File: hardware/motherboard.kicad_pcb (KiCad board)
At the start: 2 copper layers, 200 x 150 mm, 305 parts, among them J1 24 V DC input, J10 AX0: EN, STEP, DIR, GND, J11 AX1: EN, STEP, DIR, GND, J12 General outputs 0-7; pin9 fie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, J13 Encoder 0: +5,A,B,Z,GND, J14 Encoder 1: +5,A,B,Z,GND, J15 Encoder 2: +5,A,B,Z,GND, J16 Keyboard KIN0-7 / KOUT0-7, J17 Keyboard power/reference, J18 I2C0, J19 Full-size SD, SPI, J20 ESP-01S socket, J22 LCD LVDS 2x10, 2.00 mm, J23 HDMI Type A, J24 AI0/GND/AI1/GND/AI2/GND, J25 0-10 V outputs 0-3; pin 1 = c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, J26 Dedicated START button input, J27 Expansion inputs 4-7; 1=GND, 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, J28 AX2: EN, STEP, DIR, GND, J29 AX3: EN, STEP, DIR, GND, J30 AX4: EN, STEP, DIR, GND, J31 Motion AUX open-drain output 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, J4 SWD, J5 Dedicated E-stop loop, J6 Dedicated HOLD button input, J7 PLC inputs 1-8; alternating i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, J8 PLC inputs 9-16; alternating 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, J9 Expansion inputs 0-3; 1=GND, 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, Q1 DMP1045U-7, Q5 BSS138, SW2 ESP_PROG, U1 LMR36510ADDAR, U10 74HC595D, U11 74HC595D, U12 74HC595D, U13 74HC595D, U18 LTV-847S, U19 LTV-847S, U2 AMS1117-3.3, U20 LTV-847S, U21 LTV-847S, U24 SN74AHCT541DW, U25 SN74AHCT541DW, U26 ULN2003ADR, U27 ULN2003ADR, U28 SN74AHCT541DW, U30 TPD4E05U06DQA, U31 TPD4E05U06DQA, U32 TPD4E05U06DQA, U34 AMS1117-3.3, U35 EL3H7, U36 EL3H7, U37 L78L12ACUTR, U38 TLV2374IDR, U39 EL3H7, U40 TBA2-0512, U6 74HC165D, U7 74HC165D, U8 74HC165D, U9 74HC165D

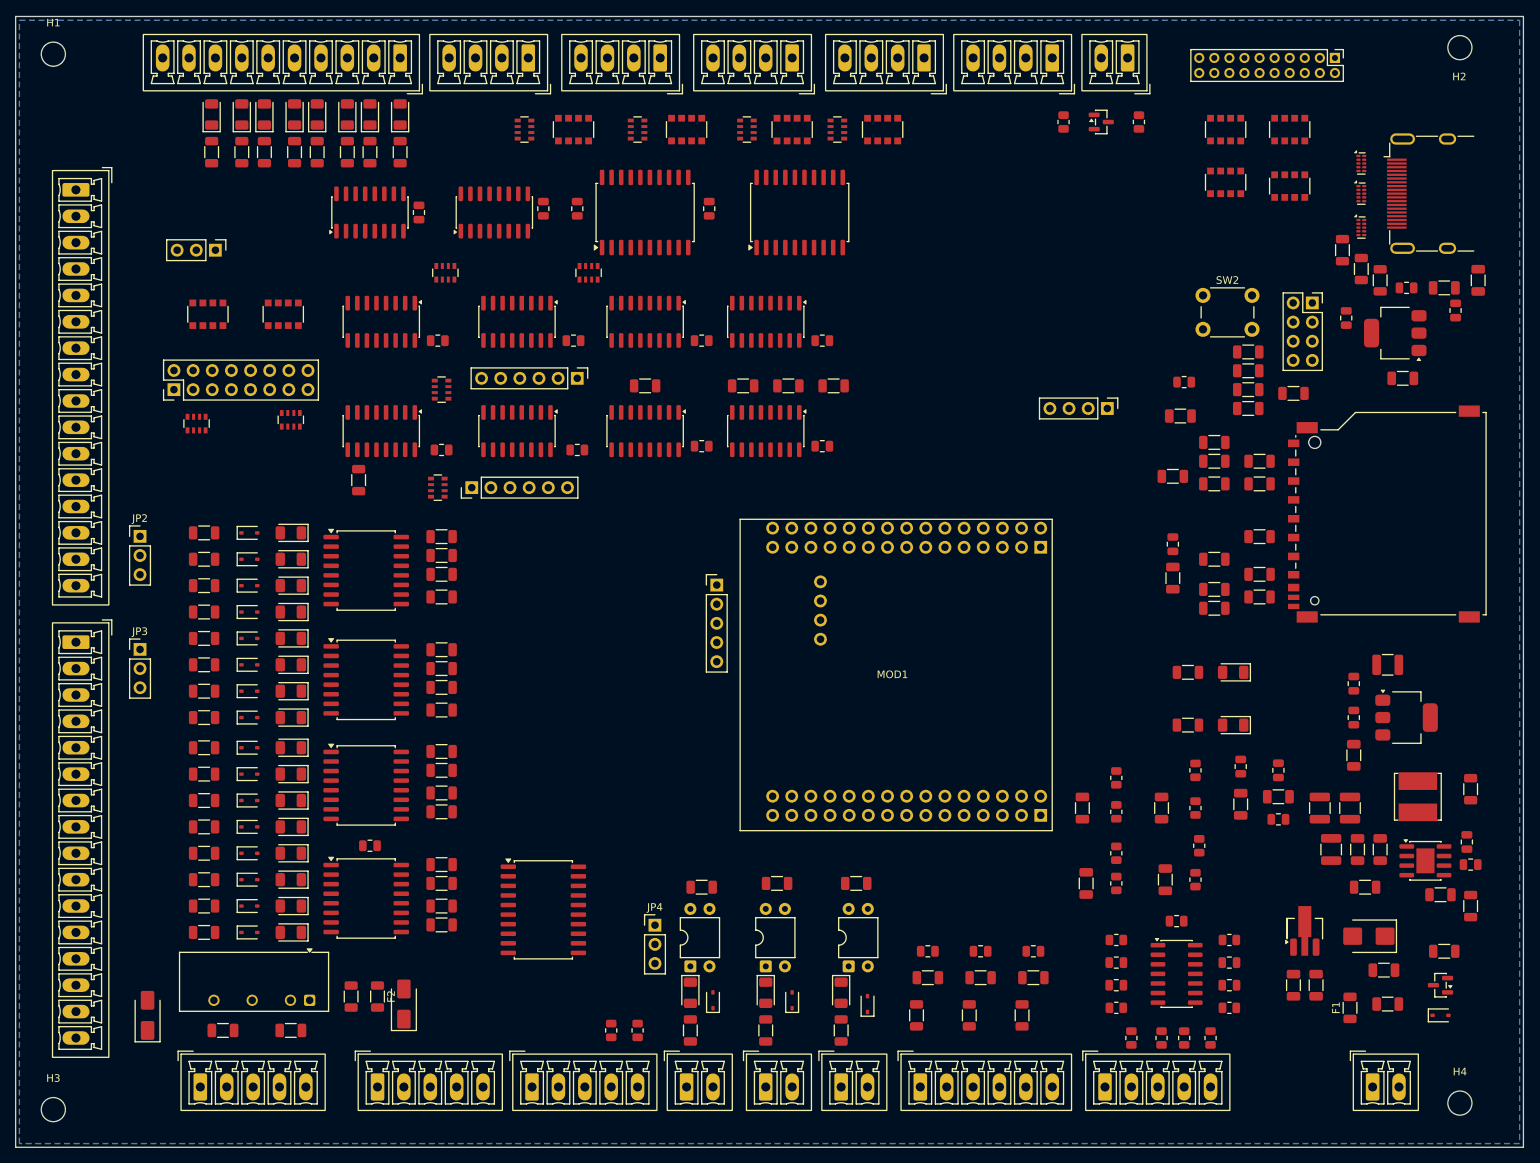
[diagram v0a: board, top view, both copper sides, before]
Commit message: Update RP2350B PCB, pinout and fabrication rules
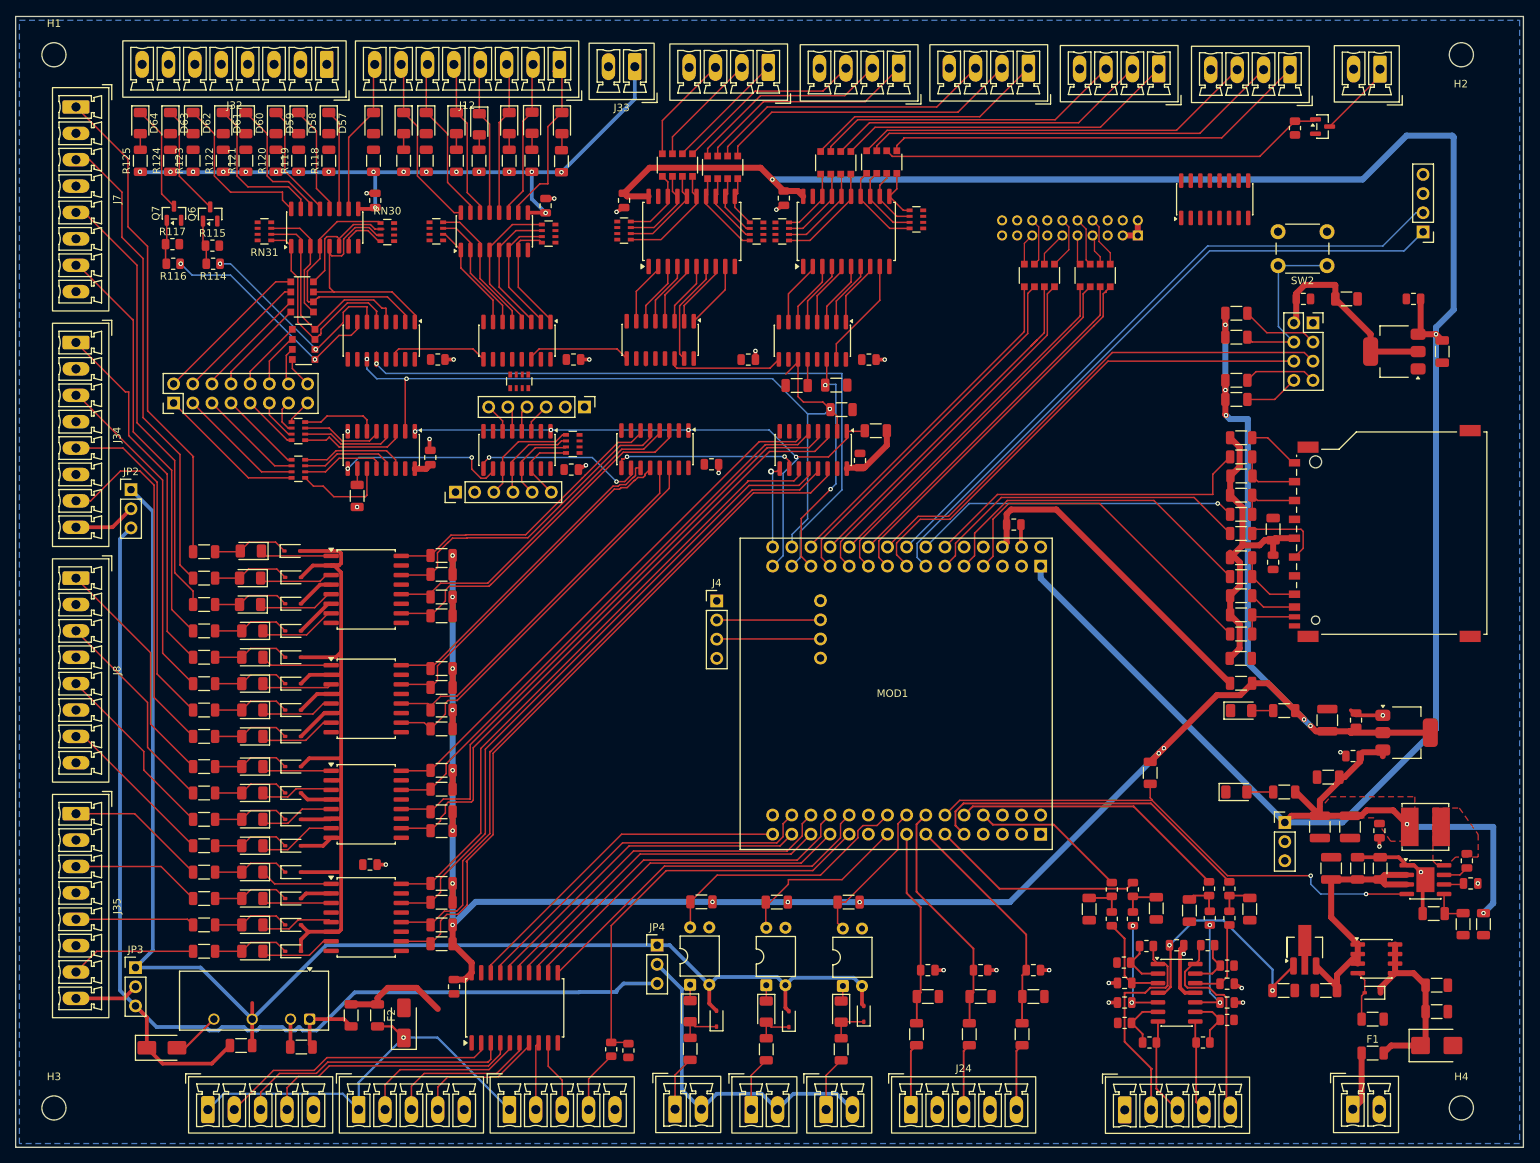
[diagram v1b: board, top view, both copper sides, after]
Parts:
- removed C14, C16, C71, C8: 10uF, C_1206_3216Metric
- removed C17, C72, C77: 100nF, C_0805_2012Metric
- removed F3: 500mA, R_1206_3216Metric
- removed J23: HDMI Type A, HDMI_A_Molex_208658-1001_Horizontal
- removed R112: 100R, R_0805_2012Metric
- removed R59, R60: 4.7k, R_1206_3216Metric
- removed RN28, RN29: 4x0R, R_Array_Convex_4x1206
- removed U30, U31, U32: TPD4E05U06DQA, USON-10_2.5x1.0mm_P0.5mm
- added C106: 100nF, C_0805_2012Metric, F.Cu at (58.1, 128.7)
- added D57: DO8, LED_1206_3216Metric, F.Cu at (41.5, 14.1)
- added D58: DO9, LED_1206_3216Metric, F.Cu at (37.5, 14.1)
- added D59: DO10, LED_1206_3216Metric, F.Cu at (34.5, 14.1)
- added D60: DO11, LED_1206_3216Metric, F.Cu at (30.5, 14.1)
- added D61: DO12, LED_1206_3216Metric, F.Cu at (27.5, 14.1)
- added D62: DO13, LED_1206_3216Metric, F.Cu at (23.5, 14.1)
- added D63: DO14, LED_1206_3216Metric, F.Cu at (20.5, 14.1)
- added D64: DO15, LED_1206_3216Metric, F.Cu at (16.5, 14.1)
- added J32: General outputs 8-15; DO_COM and GND are shared through J12, PhoenixContact_MCV_1,5_8-G-3.5_1x08_P3.50mm_Vertical, F.Cu at (41.3, 6.35)
- added J33: General outputs field +V and GND, PhoenixContact_MCV_1,5_2-G-3.5_1x02_P3.50mm_Vertical, F.Cu at (82.1, 6.66)
- added J34: PLC positions 5-8 of J7 bank; software-mapped isolated inpu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, PhoenixContact_MCV_1,5_8-G-3.5_1x08_P3.50mm_Vertical, F.Cu at (8.00, 43.2)
- added J35: PLC positions 5-8 of J8 bank; software-mapped isolated inpu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, PhoenixContact_MCV_1,5_8-G-3.5_1x08_P3.50mm_Vertical, F.Cu at (8.00, 105.8)
- added Q6: BSS138, SOT-23, F.Cu at (25.8, 26.2)
- added Q7: BSS138, SOT-23, F.Cu at (21.0, 26.1)
- added R114: 100R, R_0805_2012Metric, F.Cu at (26.2, 32.8)
- added R115: 100k, R_0805_2012Metric, F.Cu at (26.1, 30.4)
- added R116: 100R, R_0805_2012Metric, F.Cu at (20.9, 32.8)
- added R117: 100k, R_0805_2012Metric, F.Cu at (20.8, 30.2)
- added R118: 2.2k, R_1206_3216Metric, F.Cu at (41.5, 19.1)
- added R119: 2.2k, R_1206_3216Metric, F.Cu at (37.5, 19.1)
- added R120: 2.2k, R_1206_3216Metric, F.Cu at (34.5, 19.1)
- added R121: 2.2k, R_1206_3216Metric, F.Cu at (30.5, 19.1)
- added R122: 2.2k, R_1206_3216Metric, F.Cu at (27.5, 19.1)
- added R123: 2.2k, R_1206_3216Metric, F.Cu at (23.5, 19.1)
- added R124: 2.2k, R_1206_3216Metric, F.Cu at (20.5, 19.1)
- added R125: 2.2k, R_1206_3216Metric, F.Cu at (16.5, 19.1)
- added RN30: 4x10k, R_Array_Convex_4x0603, F.Cu at (49.3, 28.6)
- added RN31: 4x10k, R_Array_Convex_4x0603, F.Cu at (33.0, 28.5)
- added U41: DS90LV047A, SOIC-16_3.9x9.9mm_P1.27mm, F.Cu at (159.1, 24.2)
- J12: footprint PhoenixContact_MCV_1,5_10-G-3.5_1x10_P3.50mm_Vertical -> PhoenixContact_MCV_1,5_8-G-3.5_1x08_P3.50mm_Vertical
- J22: moved to B.Cu
- J24: footprint PhoenixContact_MCV_1,5_6-G-3.5_1x06_P3.50mm_Vertical -> PhoenixContact_MCV_1,5_5-G-3.5_1x05_P3.50mm_Vertical
- J4: footprint PinHeader_1x05_P2.54mm_Vertical -> PinHeader_1x04_P2.54mm_Vertical
- J7, J8: footprint PhoenixContact_MCV_1,5_16-G-3.5_1x16_P3.50mm_Vertical -> PhoenixContact_MCV_1,5_8-G-3.5_1x08_P3.50mm_Vertical
- Q1: value DMP1045U-7 -> IRF7240PBF; footprint SOT-23 -> SOIC-8_3.9x4.9mm_P1.27mm
- moved J17 160.9 mm to (168.3, 106.9), turned to 0 degrees
- moved J10 101.0 mm to (169.0, 7.06)
- moved J11 66.1 mm to (151.6, 6.96)
- moved J18 48.0 mm to (186.7, 28.6), turned to 180 degrees
- moved JP3 42.2 mm to (15.9, 126.2)
- moved FB1 39.0 mm to (162.6, 88.5), turned to 180 degrees
- moved J30 37.7 mm to (99.8, 6.76)
- moved J22 35.2 mm to (148.8, 29.1), turned to 90 degrees
- moved J31 33.5 mm to (181.0, 6.99)
- moved R73 32.3 mm to (150.5, 100.3), turned to 90 degrees
- moved RN26 32.3 mm to (143.2, 34.4)
- moved RN27 31.4 mm to (135.8, 34.4)
- moved J28 31.4 mm to (134.3, 6.86)
- moved R11 31.2 mm to (114.1, 55.0)
- moved R113 30.7 mm to (169.7, 14.8), turned to -90 degrees
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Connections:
- J10 pad 1: MOTION3 -> MOTION0
- J10 pad 3: MOTION0 -> MOTION2
- J11 pad 1: MOTION4 -> MOTION3
- J11 pad 2: MOTION2 -> MOTION4
- J22 pad 1: GND -> +3V3
- J22 pad 10: GND -> LVDS_D1_P
- J22 pad 11: LVDS_D1_N -> LVDS_D2_N
- J22 pad 12: LVDS_D1_P -> LVDS_D2_P
- J22 pad 14: LVDS_D2_N -> GND
- J22 pad 15: LVDS_D2_P -> LVDS_CLK_N
- J22 pad 16: GND -> LVDS_CLK_P
- J22 pad 17: LVDS_CLK_N -> (no net)
- J22 pad 18: LVDS_CLK_P -> (no net)
- J22 pad 19: GND -> (no net)
- J22 pad 4: +3V3 -> GND
- J22 pad 5: (no net) -> GND
- J22 pad 6: BL_PWM -> GND
- J22 pad 7: (no net) -> LVDS_D0_N
- J22 pad 8: LVDS_D0_N -> LVDS_D0_P
- J22 pad 9: LVDS_D0_P -> LVDS_D1_N
- J28 pad 1: MOTION9 -> MOTION6
- J28 pad 3: MOTION6 -> MOTION8
- J29 pad 1: MOTION10 -> MOTION9
- J29 pad 2: MOTION8 -> MOTION10
- J30 pad 1: MOTION15 -> MOTION12
- J30 pad 3: MOTION12 -> MOTION14
- MOD1 pad 25: SR_LATCH -> (no net)
- MOD1 pad 4: RESET_N -> (no net)
- MOD1 pad 43: SR_SCK -> SR_OUT_SER
- MOD1 pad 44: SR_IN_Q7 -> SR_LATCH
- MOD1 pad 45: SR_OUT_SER -> SR_PL_N
- MOD1 pad 49: BL_PWM -> (no net)
- MOD1 pad 59: SR_PL_N -> SR_SCK
- MOD1 pad 60: (no net) -> SR_IN_Q7
- Q1 pad 1: Q1_GATE -> VIN_PROT
- Q1 pad 3: VIN_FUSED -> VIN_PROT
- RN10 pad 1: BUFY8 -> BUFY9
- RN10 pad 2: BUFY9 -> BUFY8
- RN11 pad 1: BUFY12 -> GND
- RN11 pad 2: BUFY13 -> GND
- RN11 pad 3: BUFY14 -> GND
- RN11 pad 4: BUFY15 -> GND
- RN11 pad 5: GND -> BUFY12
- RN11 pad 6: GND -> BUFY13
- RN11 pad 7: GND -> BUFY14
- RN11 pad 8: GND -> BUFY15
- RN12 pad 1: OUT16 -> OUT19
- RN12 pad 2: OUT17 -> OUT18
- RN12 pad 3: OUT18 -> OUT17
- RN12 pad 4: OUT19 -> OUT16
- RN13 pad 1: OUT20 -> (no net)
- RN13 pad 2: OUT21 -> OUT22
- RN13 pad 3: OUT22 -> OUT21
- RN13 pad 4: OUT23 -> OUT20
- RN13 pad 8: GND -> (no net)
- RN16 pad 6: MOTION1 -> AUX_GATE
- RN16 pad 7: MOTION2 -> MOTION1
- RN16 pad 8: MOTION3 -> MOTION2
- RN17 pad 5: MOTION4 -> MOTION3
- RN17 pad 6: MOTION5 -> MOTION4
- RN17 pad 7: MOTION6 -> MOTION5
- RN17 pad 8: MOTION7 -> MOTION6
- RN18 pad 5: MOTION8 -> MOTION7
- RN18 pad 6: MOTION9 -> MOTION8
- RN18 pad 7: MOTION10 -> MOTION9
- RN18 pad 8: MOTION11 -> MOTION10
- RN19 pad 5: MOTION12 -> MOTION11
- RN19 pad 6: MOTION13 -> MOTION12
- RN19 pad 7: MOTION14 -> MOTION13
- RN19 pad 8: MOTION15 -> MOTION14
- RN20 pad 2: OUT25 -> KOUT1
- RN20 pad 4: OUT27 -> KOUT3
- RN20 pad 5: KOUT3 -> OUT27
- RN20 pad 7: KOUT1 -> OUT25
- RN26 pad 1: HSTX_D1_P -> HSTX_D1_N
- RN26 pad 2: HSTX_D1_N -> HSTX_D1_P
- RN26 pad 3: HSTX_D0_P -> HSTX_D0_N
- RN26 pad 4: HSTX_D0_N -> HSTX_D0_P
- RN26 pad 5: LVDS_D0_N -> LVDS_D0_P
- RN26 pad 6: LVDS_D0_P -> LVDS_D0_N
- RN26 pad 7: LVDS_D1_N -> LVDS_D1_P
- RN26 pad 8: LVDS_D1_P -> LVDS_D1_N
- RN27 pad 1: HSTX_CLK_P -> HSTX_CLK_N
- RN27 pad 2: HSTX_CLK_N -> HSTX_CLK_P
- RN27 pad 3: HSTX_D2_P -> HSTX_D2_N
- RN27 pad 4: HSTX_D2_N -> HSTX_D2_P
- RN27 pad 5: LVDS_D2_N -> LVDS_D2_P
- RN27 pad 6: LVDS_D2_P -> LVDS_D2_N
- RN27 pad 7: LVDS_CLK_N -> LVDS_CLK_P
- RN27 pad 8: LVDS_CLK_P -> LVDS_CLK_N
- RN8 pad 1: BUFY0 -> GND
- RN8 pad 2: BUFY1 -> GND
- RN8 pad 3: BUFY2 -> GND
- RN8 pad 4: BUFY3 -> GND
- RN8 pad 5: GND -> BUFY1
- RN8 pad 6: GND -> BUFY0
- RN8 pad 7: GND -> BUFY3
- RN8 pad 8: GND -> BUFY2
- RN9 pad 1: BUFY4 -> BUFY5
- RN9 pad 2: BUFY5 -> BUFY4
- RN9 pad 3: BUFY6 -> BUFY7
- RN9 pad 4: BUFY7 -> BUFY6
- U10 pad 10: RESET_N -> +3V3
- U11 pad 10: RESET_N -> +3V3
- U12 pad 10: RESET_N -> +3V3
- U13 pad 10: RESET_N -> +3V3
- U26 pad 1: OUT19 -> OUT22
- U26 pad 10: (no net) -> DO0
- U26 pad 11: (no net) -> DO1
- U26 pad 12: (no net) -> DO2
- U26 pad 13: DO0 -> DO3
- U26 pad 14: DO1 -> DO4
- U26 pad 15: DO2 -> DO5
- U26 pad 16: DO3 -> DO6
- U26 pad 2: OUT18 -> OUT21
- U26 pad 3: OUT17 -> OUT20
- U26 pad 4: OUT16 -> OUT19
- U26 pad 5: (no net) -> OUT18
- U26 pad 6: (no net) -> OUT17
- U26 pad 7: (no net) -> OUT16
- U27 pad 1: OUT23 -> OUT29
- U27 pad 10: (no net) -> DO7
- U27 pad 11: (no net) -> DO8
- U27 pad 12: (no net) -> DO9
- U27 pad 13: DO4 -> DO10
- U27 pad 14: DO5 -> DO11
- U27 pad 15: DO6 -> DO12
- U27 pad 16: DO7 -> DO13
- U27 pad 2: OUT22 -> OUT28
- U27 pad 3: OUT21 -> OUT27
- U27 pad 4: OUT20 -> OUT26
- U27 pad 5: (no net) -> OUT25
- U27 pad 6: (no net) -> OUT24
- U27 pad 7: (no net) -> OUT23
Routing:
- net +5V: track 0.00 -> 358.2 mm, vias 0 -> 4
- net ISO_GND: track 0.00 -> 328.2 mm
- net +3V3: track 0.00 -> 303.3 mm, vias 0 -> 18
- net +12V_FIELD: track 0.00 -> 158.3 mm
- net SR_SCK: track 0.00 -> 109.5 mm, vias 0 -> 3
- net SR_LATCH: track 0.00 -> 96.4 mm, vias 0 -> 1
- net PLC_IN8_N: track 0.00 -> 94.3 mm
- net PLC_IN7_N: track 0.00 -> 90.6 mm
- net DO_COM: track 0.00 -> 89.7 mm, vias 0 -> 18
- net I2C_SDA: track 0.00 -> 87.7 mm
- net I2C_SCL: track 0.00 -> 87.6 mm
- net PLC_IN6_N: track 0.00 -> 86.1 mm
- net PLC_IN4_N: track 0.00 -> 84.1 mm
- net PLC_IN5_N: track 0.00 -> 82.8 mm
- net PLC_IN3_N: track 0.00 -> 81.1 mm
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- added copper zone on F.Cu, net +5V
- added copper zone on F.Cu, net BUCK5_SW

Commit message: Finalize interface routing and repair PCB connectivity
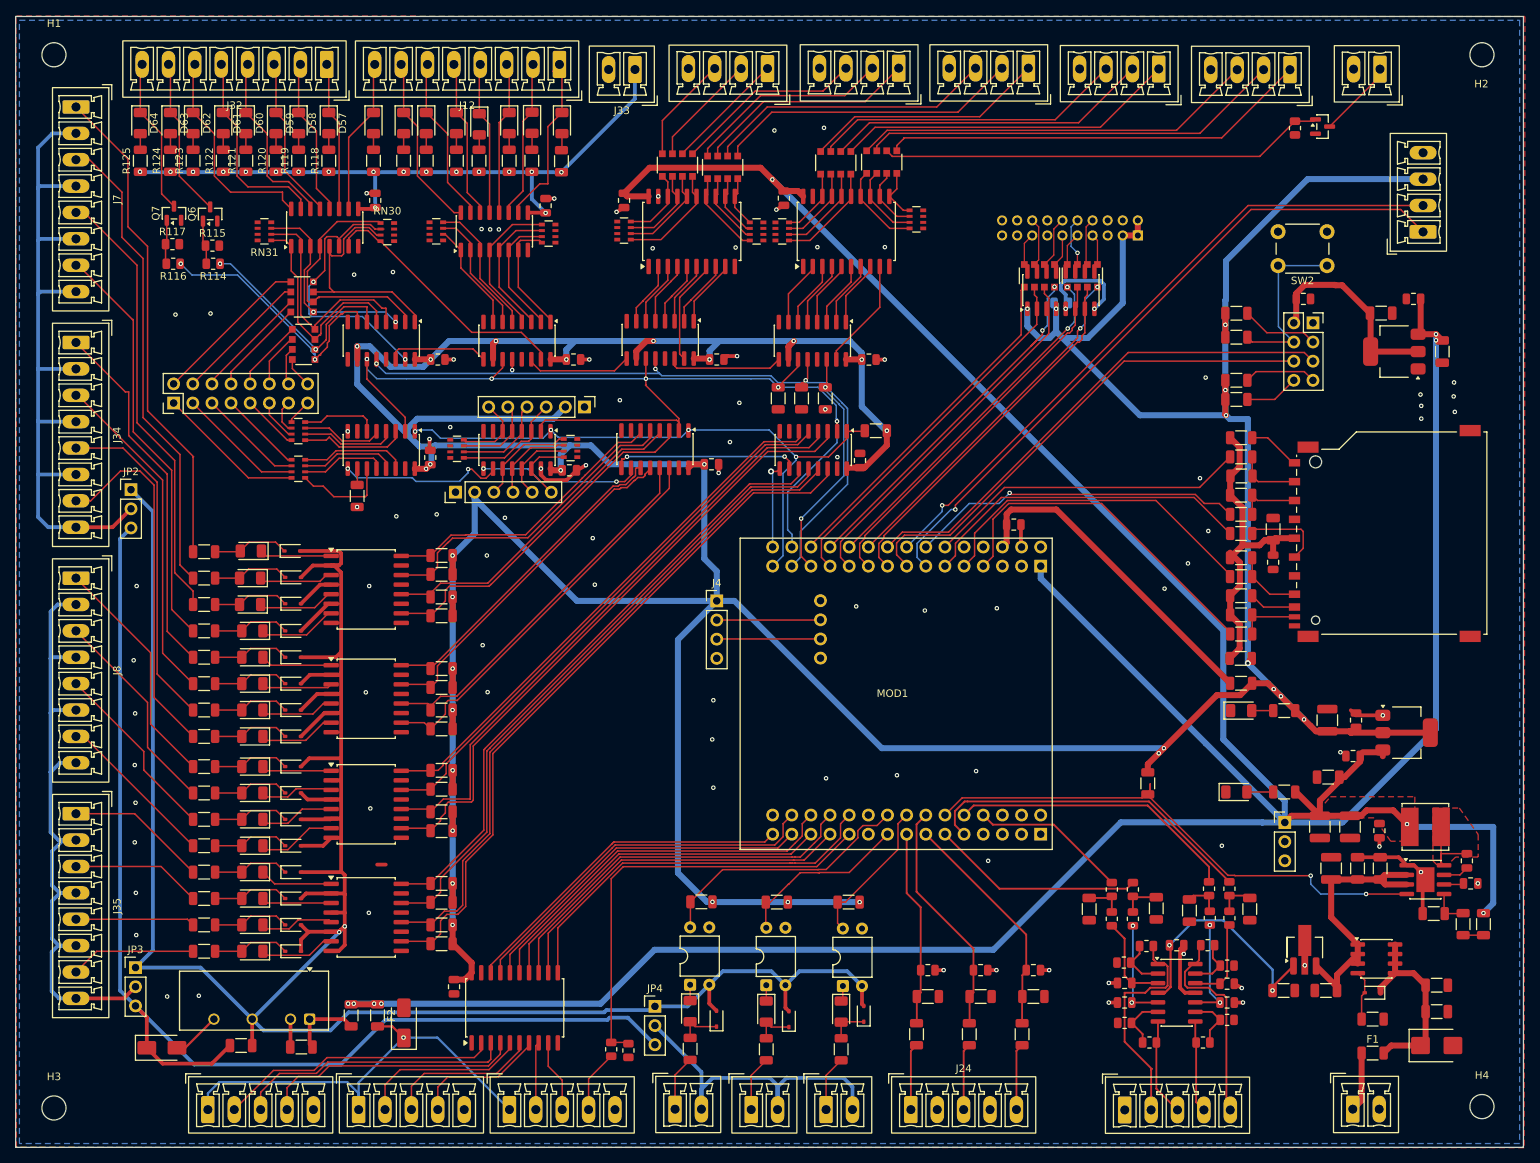
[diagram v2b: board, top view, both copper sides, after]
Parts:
- C57: moved to B.Cu
- J18: footprint PinHeader_1x04_P2.54mm_Vertical -> PhoenixContact_MCV_1,5_4-G-3.5_1x04_P3.50mm_Vertical
- moved C57 118.1 mm to (138.7, 38.0)
- moved U41 23.7 mm to (138.7, 36.3)
- moved RN7 12.2 mm to (58.5, 57.4), turned to 180 degrees
- moved R10 8.53 mm to (101.2, 50.6), turned to -90 degrees
- moved JP4 8.13 mm to (84.8, 131.3)
- moved C69 4.97 mm to (181.1, 39.4)
- moved C27 4.18 mm to (93.0, 45.5)
- moved H4 2.74 mm to (194.5, 144.6)
- moved H2 2.73 mm to (194.5, 5.08)
- moved R12 2.27 mm to (107.4, 50.6), turned to -90 degrees
- moved R13 1.82 mm to (104.2, 50.6), turned to -90 degrees
- moved RN26 1.70 mm to (141.5, 34.4)
- moved R73 1.43 mm to (150.2, 101.7)
- moved RN6 0.63 mm to (73.6, 57.2)
- moved J33 0.38 mm to (82.2, 7.03)
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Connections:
- RN26 pad 3: HSTX_D0_N -> HSTX_D0_P
- RN26 pad 4: HSTX_D0_P -> HSTX_D0_N
- RN26 pad 5: LVDS_D0_P -> LVDS_D0_N
- RN26 pad 6: LVDS_D0_N -> LVDS_D0_P
- RN27 pad 3: HSTX_D2_N -> HSTX_D2_P
- RN27 pad 4: HSTX_D2_P -> HSTX_D2_N
- RN27 pad 5: LVDS_D2_P -> LVDS_D2_N
- RN27 pad 6: LVDS_D2_N -> LVDS_D2_P
- U41 pad 2: HSTX_D0_P -> HSTX_CLK_P
- U41 pad 3: HSTX_D1_P -> HSTX_D2_P
- U41 pad 6: HSTX_D2_P -> HSTX_D1_P
- U41 pad 7: HSTX_CLK_P -> HSTX_D0_P
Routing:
- net +3V3: track 303.3 -> 696.6 mm, vias 18 -> 35
- net +5V: track 358.2 -> 475.3 mm, vias 4 -> 9
- net FIELD_COM0: track 8.31 -> 99.2 mm
- net FIELD_COM1: track 8.54 -> 92.7 mm
- net SR_SCK: track 109.5 -> 142.0 mm, vias 3 -> 5
- net OUT23: track 6.28 -> 34.6 mm
- net ISO_GND: track 328.2 -> 355.7 mm, vias 0 -> 2
- net GND: track 58.0 -> 79.4 mm, vias 27 -> 94
- net OUT24: track 16.4 -> 36.2 mm, vias 0 -> 2
- net OUT27: track 16.3 -> 27.8 mm, vias 0 -> 2
- net EXP_IN4: track 4.04 -> 15.0 mm
- net BUCK5_SW: track 0.00 -> 9.80 mm
- net EXP_IN5: track 3.51 -> 12.5 mm
- net EXP_IN6: track 3.46 -> 10.9 mm
- net DO12: track 20.2 -> 26.7 mm
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- added copper zone on F.Cu, net GND
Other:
- board text added: "1-3: 3V3"
- board text added: "11/12: D2- / D2+"
- board text added: "15/16: CLK- / CLK+"
- board text added: "17-20: NC"
- board text added: "4-6,13-14: GND"
- board text added: "7/8: D0- / D0+"
- board text added: "9/10: D1- / D1+"
- board text added: "J22 LCD LVDS 2x10"
